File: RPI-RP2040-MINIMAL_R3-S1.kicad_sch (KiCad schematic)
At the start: 38 parts, among them J3 Conn_01x04_Pin, J4 Conn_01x04_Socket, P1 USB_C_Plug_USB2.0, U1 NCP1117ST33T3G, U2 W25Q128JVSIQ, U3 RP2040, X1 12MHz

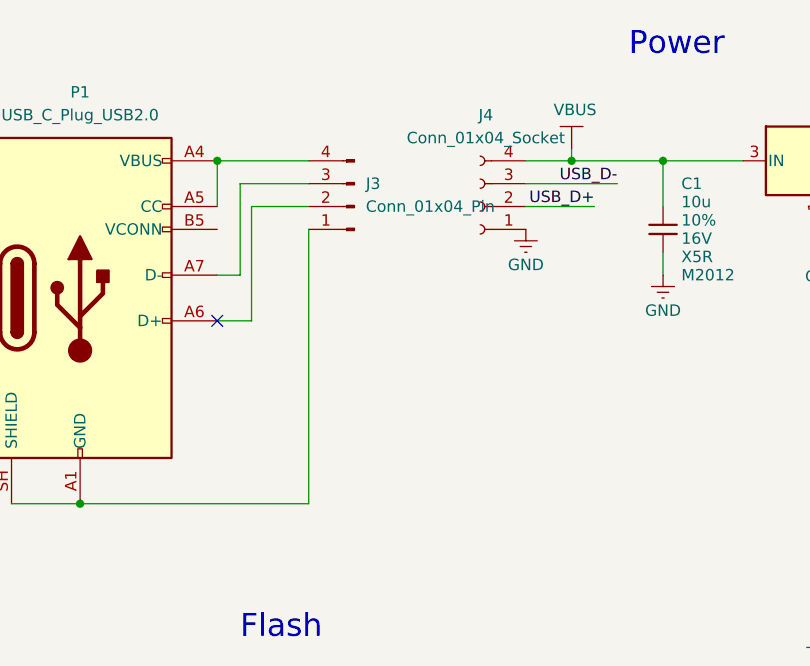
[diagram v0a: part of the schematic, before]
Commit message: flip connector in schematic but not pcb i cant update pcb pls help
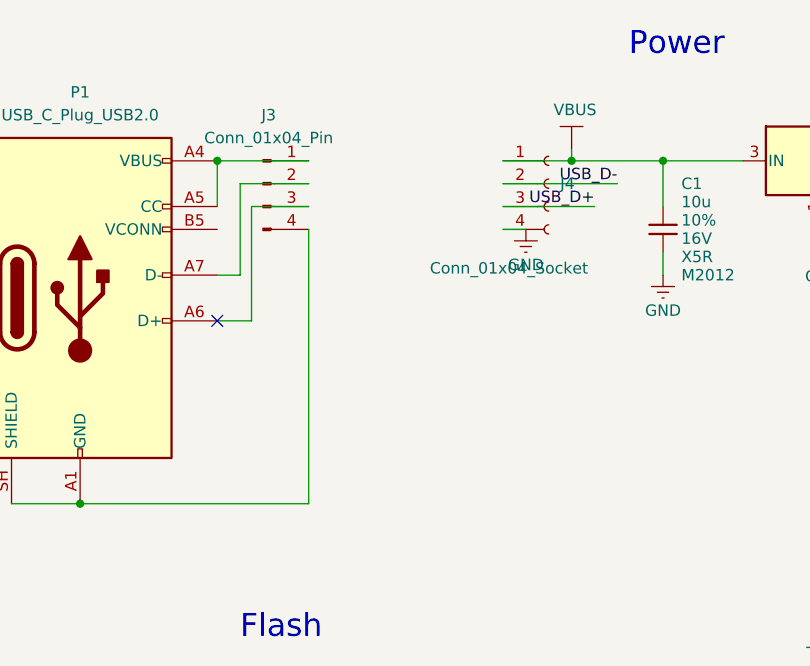
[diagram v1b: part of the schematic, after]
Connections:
- net GND: now also J4.4 (Pin_4); no longer J4.1 (Pin_1)
- net USB_D+: now also J4.3 (Pin_3); no longer J4.2 (Pin_2)
- net USB_D-: now also J4.2 (Pin_2); no longer J4.3 (Pin_3)
- net VBUS: now also J4.1 (Pin_1); no longer J4.4 (Pin_4)
- net at P1.A1 (GND), P1.A12 (GND), P1.B1 (GND)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: now also J3.4 (Pin_4); no longer J3.1 (Pin_1)
- net at J3.2 (Pin_2): now also P1.A7 (D-); no longer P1.A6 (D+)
- net at J3.3 (Pin_3): now also P1.A6 (D+); no longer P1.A7 (D-)
- net at P1.A4 (VBUS), P1.A5 (CC), P1.A9 (VBUS)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: now also J3.1 (Pin_1); no longer J3.4 (Pin_4)
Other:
- moved on the sheet: J3, J4
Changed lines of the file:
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@@
 	)
 	(junction
-		(at 83.82 45.72)
-		(diameter 0)
-		(color 0 0 0 0)
-	)
-	(junction
 		(at 234.95 50.8)
 		(diameter 0)
@@
 	)
 	(junction
+		(at 83.82 45.72)
+		(diameter 0)
+		(color 0 0 0 0)
+	)
+	(junction
 		(at 68.58 227.33)
 		(diameter 0)
@@
 	(wire
 		(pts
-			(xy 88.9 48.26) (xy 78.74 48.26)
+			(xy 88.9 48.26) (xy 76.2 48.26)
 		)
 		(stroke
@@
 	(wire
 		(pts
-			(xy 78.74 45.72) (xy 83.82 45.72)
+			(xy 76.2 45.72) (xy 83.82 45.72)
 		)
 		(stroke
@@
 	(wire
 		(pts
-			(xy 54.61 83.82) (xy 54.61 53.34)
-		)
-		(stroke
-			(width 0)
-			(type default)
-		)
-	)
-	(wire
-		(pts
 			(xy 228.6 130.81) (xy 243.84 130.81)
 		)
@@
 	(wire
 		(pts
-			(xy 78.74 50.8) (xy 86.36 50.8)
+			(xy 76.2 50.8) (xy 86.36 50.8)
 		)
 		(stroke
@@
 	(wire
 		(pts
+			(xy 54.61 53.34) (xy 54.61 83.82)
+		)
+		(stroke
+			(width 0)
+			(type default)
+		)
+	)
+	(wire
+		(pts
 			(xy 212.09 175.26) (xy 212.09 190.5)
 		)
@@
 	(wire
 		(pts
+			(xy 76.2 53.34) (xy 78.74 53.34)
+		)
+		(stroke
+			(width 0)
+			(type default)
+		)
+	)
+	(wire
+		(pts
 			(xy 351.79 186.69) (xy 351.79 190.5)
 		)
@@
 	(symbol
 		(lib_id "Connector:Conn_01x04_Pin")
-		(at 59.69 50.8 180)
+		(at 49.53 48.26 0)
 		(unit 1)
 		(body_style 1)
@@
 		(fields_autoplaced yes)
 		(property "Reference" "J3"
-			(at 60.96 48.2599 0)
+			(at 50.165 40.64 0)
 			(show_name no)
 			(do_not_autoplace no)
@@
 					(size 1.27 1.27)
 				)
-				(justify right)
 			)
 		)
 		(property "Value" "Conn_01x04_Pin"
-			(at 60.96 50.7999 0)
+			(at 50.165 43.18 0)
 			(show_name no)
 			(do_not_autoplace no)
@@
 					(size 1.27 1.27)
 				)
-				(justify right)
 			)
 		)
 		(property "Footprint" "Connector_PinHeader_2.54mm:PinHeader_1x04_P2.54mm_Horizontal"
-			(at 59.69 50.8 0)
+			(at 49.53 48.26 0)
 			(hide yes)
 			(show_name no)
@@
 		)
 		(property "Datasheet" ""
-			(at 59.69 50.8 0)
+			(at 49.53 48.26 0)
 			(hide yes)
 			(show_name no)
@@
 		)
 		(property "Description" "Generic connector, single row, 01x04, script generated"
-			(at 59.69 50.8 0)
+			(at 49.53 48.26 0)
 			(hide yes)
 			(show_name no)
@@
 	(symbol
 		(lib_id "Connector:Conn_01x04_Socket")
-		(at 73.66 50.8 180)
+		(at 81.28 48.26 0)
 		(unit 1)
 		(body_style 1)
@@
 		(in_pos_files yes)
 		(dnp no)
-		(fields_autoplaced yes)
 		(property "Reference" "J4"
-			(at 74.295 40.64 0)
+			(at 82.55 48.2599 0)
 			(show_name no)
 			(do_not_autoplace no)
@@
 					(size 1.27 1.27)
 				)
+				(justify left)
 			)
 		)
 		(property "Value" "Conn_01x04_Socket"
-			(at 74.295 43.18 0)
+			(at 68.072 57.6579 0)
 			(show_name no)
 			(do_not_autoplace no)
@@
 					(size 1.27 1.27)
 				)
+				(justify left)
 			)
 		)
 		(property "Footprint" "Connector_PinSocket_2.54mm:PinSocket_1x04_P2.54mm_Vertical"
-			(at 73.66 50.8 0)
+			(at 81.28 48.26 0)
 			(hide yes)
 			(show_name no)
@@
 		)
 		(property "Datasheet" ""
-			(at 73.66 50.8 0)
+			(at 81.28 48.26 0)
 			(hide yes)
 			(show_name no)
@@
 		)
 		(property "Description" "Generic connector, single row, 01x04, script generated"
-			(at 73.66 50.8 0)
+			(at 81.28 48.26 0)
 			(hide yes)
 			(show_name no)

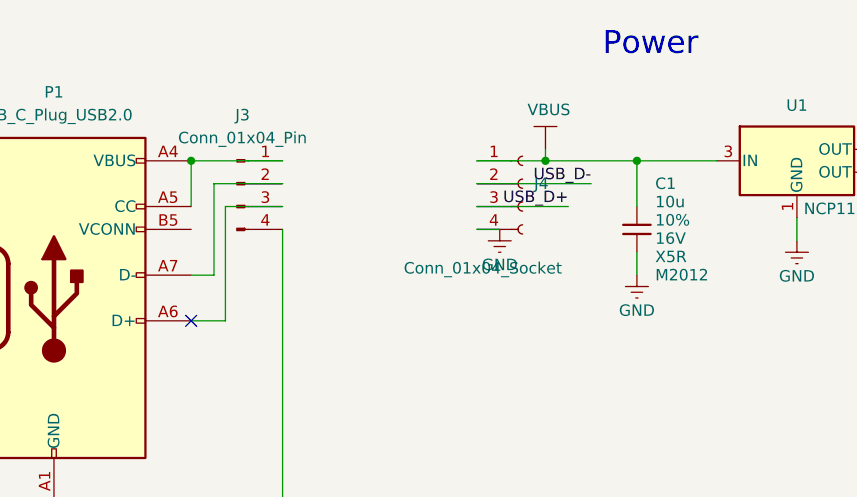
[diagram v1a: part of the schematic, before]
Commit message: swap connectors, fix button position
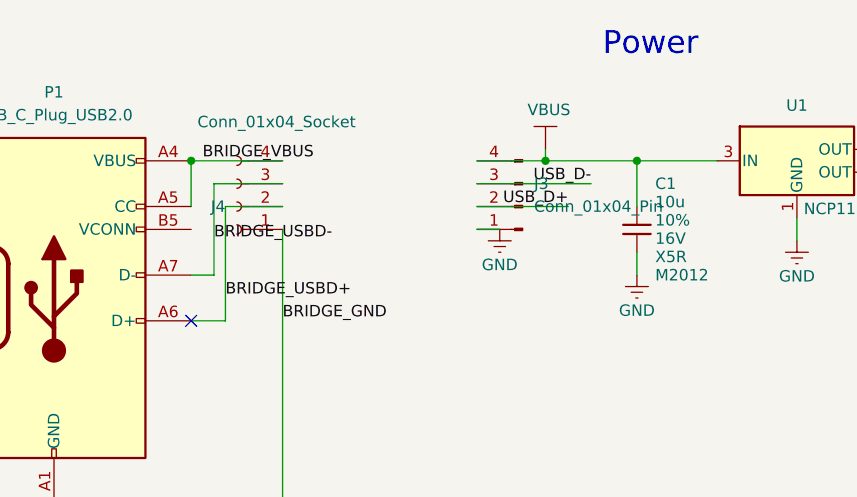
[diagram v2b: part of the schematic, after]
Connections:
- net GND: now also J3.1 (Pin_1); no longer J4.4 (Pin_4)
- net USB_D+: now also J3.2 (Pin_2); no longer J4.3 (Pin_3)
- net USB_D-: now also J3.3 (Pin_3); no longer J4.2 (Pin_2)
- net VBUS: now also J3.4 (Pin_4); no longer J4.1 (Pin_1)
- net BRIDGE_VBUS: now reaches P1.A4 (VBUS), P1.A5 (CC), P1.A9 (VBUS), P1.B4 (VBUS), P1.B9 (VBUS)
- net BRIDGE_VBUS: now also J4.4 (Pin_4); no longer J3.1 (Pin_1)
- net BRIDGE_USBD-: now reaches P1.A7 (D-)
- net BRIDGE_USBD-: now also J4.3 (Pin_3); no longer J3.2 (Pin_2)
- net BRIDGE_USBD+: now reaches P1.A6 (D+)
- net BRIDGE_USBD+: now also J4.2 (Pin_2); no longer J3.3 (Pin_3)
- net BRIDGE_GND: now reaches P1.A1 (GND), P1.A12 (GND), P1.B1 (GND), P1.B12 (GND), P1.SH (SHIELD)
- net BRIDGE_GND: now also J4.1 (Pin_1); no longer J3.4 (Pin_4)
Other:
- moved on the sheet: J3, J4
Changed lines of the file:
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@@
 	)
 	(junction
+		(at 83.82 45.72)
+		(diameter 0)
+		(color 0 0 0 0)
+	)
+	(junction
 		(at 265.43 36.83)
 		(diameter 0)
@@
 	)
 	(junction
-		(at 83.82 45.72)
-		(diameter 0)
-		(color 0 0 0 0)
-	)
-	(junction
 		(at 68.58 227.33)
 		(diameter 0)
@@
 		)
 	)
+	(label "BRIDGE_VBUS"
+		(at 45.72 45.72 0)
+		(effects
+			(font
+				(size 1.27 1.27)
+			)
+			(justify left bottom)
+		)
+	)
 	(label "GPIO21"
 		(at 243.84 153.67 180)
@@
 		)
 	)
+	(label "BRIDGE_USBD+"
+		(at 48.26 60.96 0)
+		(effects
+			(font
+				(size 1.27 1.27)
+			)
+			(justify left bottom)
+		)
+	)
 	(label "QSPI_SCLK"
 		(at 191.77 100.33 270)
@@
 		)
 	)
+	(label "BRIDGE_GND"
+		(at 54.61 63.5 0)
+		(effects
+			(font
+				(size 1.27 1.27)
+			)
+			(justify left bottom)
+		)
+	)
 	(label "GPIO12"
 		(at 181.61 190.5 90)
@@
 		)
 	)
+	(label "BRIDGE_USBD-"
+		(at 46.99 54.61 0)
+		(effects
+			(font
+				(size 1.27 1.27)
+			)
+			(justify left bottom)
+		)
+	)
 	(label "~{USB_BOOT}"
 		(at 31.75 125.73 0)
@@
 	(symbol
 		(lib_id "Connector:Conn_01x04_Pin")
-		(at 49.53 48.26 0)
+		(at 81.28 50.8 180)
 		(unit 1)
 		(body_style 1)
@@
 		(fields_autoplaced yes)
 		(property "Reference" "J3"
-			(at 50.165 40.64 0)
+			(at 82.55 48.2599 0)
 			(show_name no)
 			(do_not_autoplace no)
@@
 					(size 1.27 1.27)
 				)
+				(justify right)
 			)
 		)
 		(property "Value" "Conn_01x04_Pin"
-			(at 50.165 43.18 0)
+			(at 82.55 50.7999 0)
 			(show_name no)
 			(do_not_autoplace no)
@@
 					(size 1.27 1.27)
 				)
+				(justify right)
 			)
 		)
 		(property "Footprint" "Connector_PinHeader_2.54mm:PinHeader_1x04_P2.54mm_Horizontal"
-			(at 49.53 48.26 0)
+			(at 81.28 50.8 0)
 			(hide yes)
 			(show_name no)
@@
 		)
 		(property "Datasheet" ""
-			(at 49.53 48.26 0)
+			(at 81.28 50.8 0)
 			(hide yes)
 			(show_name no)
@@
 		)
 		(property "Description" "Generic connector, single row, 01x04, script generated"
-			(at 49.53 48.26 0)
+			(at 81.28 50.8 0)
 			(hide yes)
 			(show_name no)
@@
 	(symbol
 		(lib_id "Connector:Conn_01x04_Socket")
-		(at 81.28 48.26 0)
+		(at 49.53 50.8 180)
 		(unit 1)
 		(body_style 1)
@@
 		(dnp no)
 		(property "Reference" "J4"
-			(at 82.55 48.2599 0)
+			(at 48.26 50.8001 0)
 			(show_name no)
 			(do_not_autoplace no)
@@
 		)
 		(property "Value" "Conn_01x04_Socket"
-			(at 68.072 57.6579 0)
+			(at 62.738 41.4021 0)
 			(show_name no)
 			(do_not_autoplace no)
@@
 		)
 		(property "Footprint" "Connector_PinSocket_2.54mm:PinSocket_1x04_P2.54mm_Vertical"
-			(at 81.28 48.26 0)
+			(at 49.53 50.8 0)
 			(hide yes)
 			(show_name no)
@@
 		)
 		(property "Datasheet" ""
-			(at 81.28 48.26 0)
+			(at 49.53 50.8 0)
 			(hide yes)
 			(show_name no)
@@
 		)
 		(property "Description" "Generic connector, single row, 01x04, script generated"
-			(at 81.28 48.26 0)
+			(at 49.53 50.8 0)
 			(hide yes)
 			(show_name no)

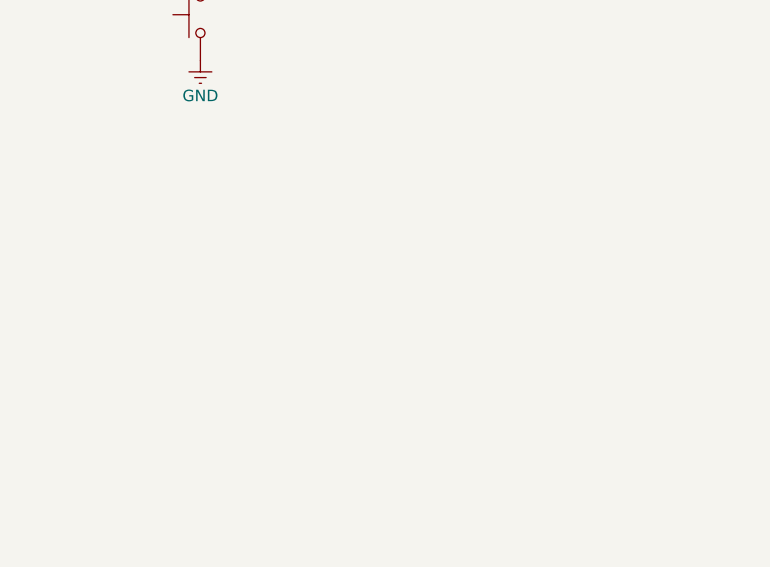
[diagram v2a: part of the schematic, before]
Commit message: switch to 2mb flash + debug port
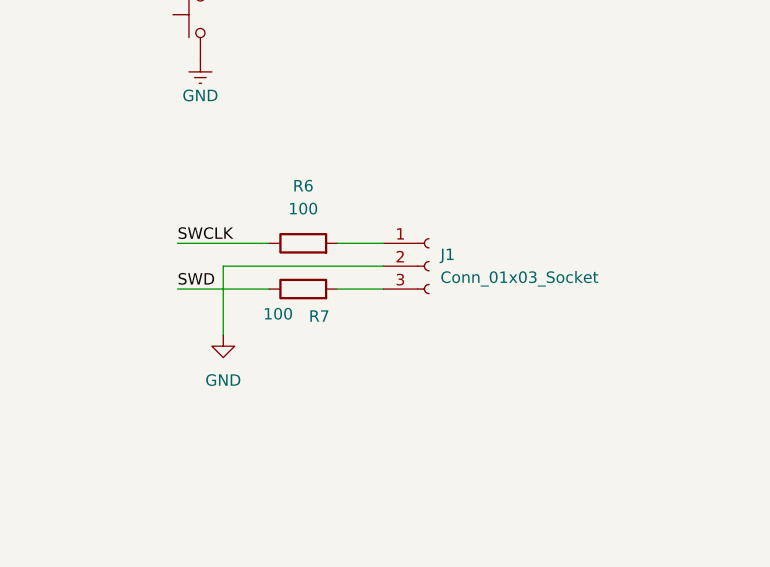
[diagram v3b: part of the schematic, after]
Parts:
- added J1: Conn_01x03_Socket, Connector_PinHeader_1.00mm:PinHeader_1x03_P1.00mm_Vertical, symbol Connector:Conn_01x03_Socket
- added R6, R7: 100, Resistor_SMD:R_0402_1005Metric, symbol Device:R
- U2: capacity 128Mbit -> 16Mbit; manufacturer_pn W25Q128JVSIQ -> W25Q16JVUXIQ
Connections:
- net GND: now also J1.2 (Pin_2)
- net SWCLK: now also R6.1
- net SWD: now also R7.1
- new net: J1.3 (Pin_3), R7.2
- new net: J1.1 (Pin_1), R6.2
